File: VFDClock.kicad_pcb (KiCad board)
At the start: 2 copper layers, 68.6 x 53.3 mm, 8 parts, among them P1 Power, P2 Analog, P3 Digital, P4 Digital, P5 CONN_01X01, P6 CONN_01X01, P7 CONN_01X01, P8 CONN_01X01

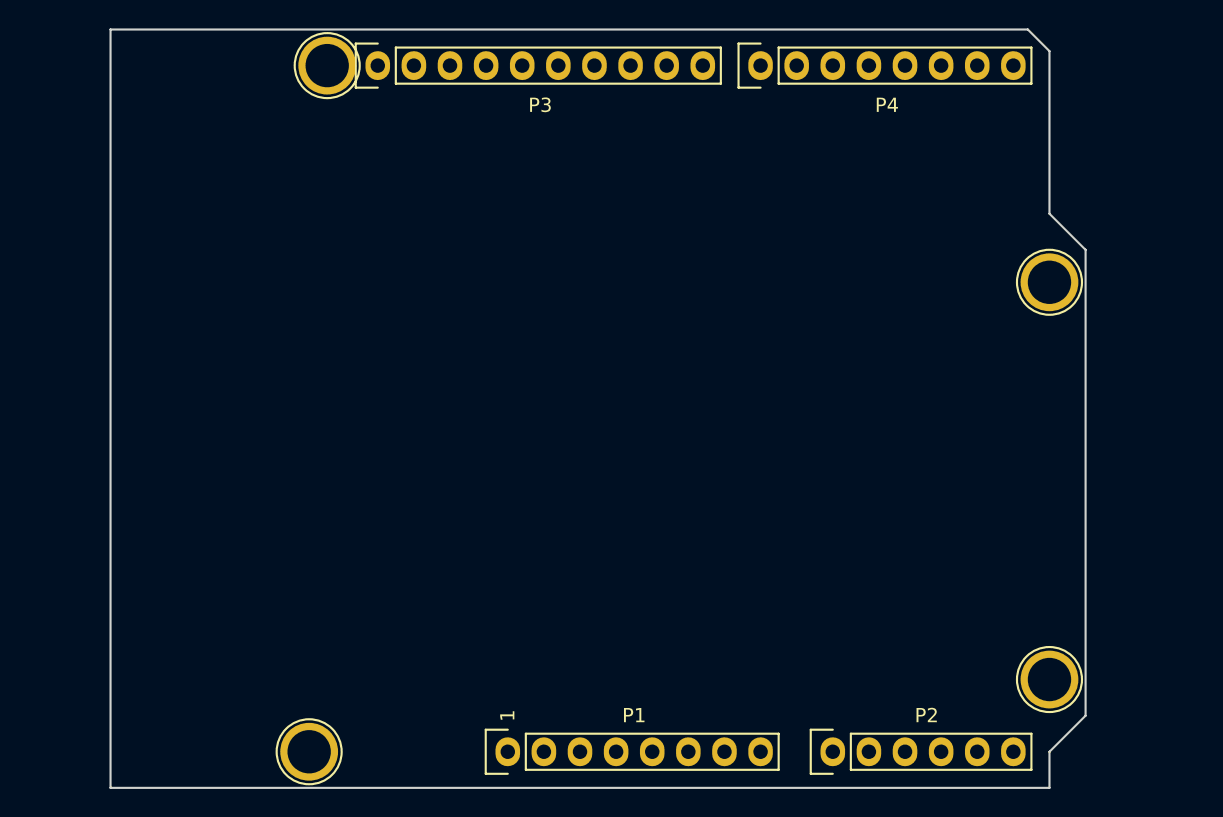
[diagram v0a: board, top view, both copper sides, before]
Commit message: VFDとICをつないだ回路を作成
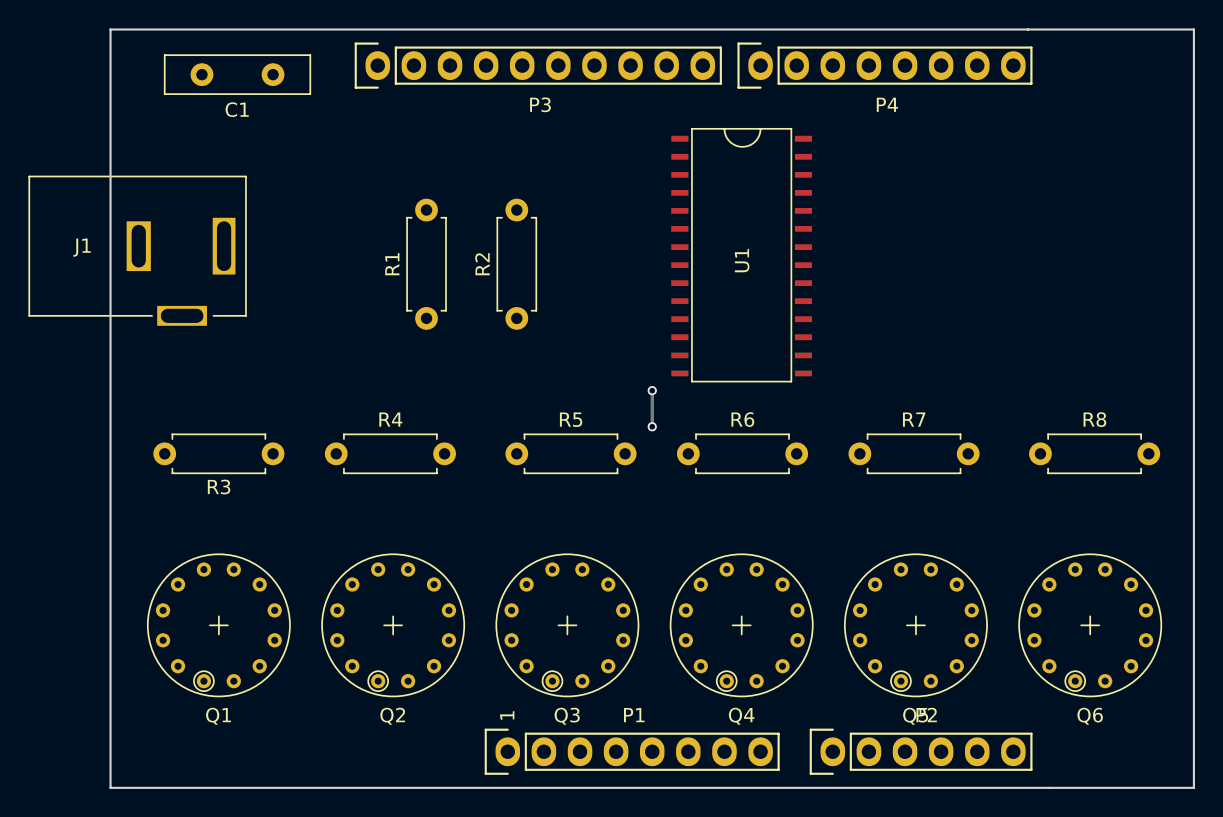
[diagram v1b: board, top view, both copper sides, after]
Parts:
- removed P5, P6, P7, P8: CONN_01X01, Socket_Arduino_Uno:Arduino_1pin
- added C1: 0.1u, Capacitor_THT:C_Disc_D10.0mm_W2.5mm_P5.00mm, F.Cu at (122.4, 76.2)
- added J1: Barrel_Jack_MountingPin, #MyFootPrints:DCJack_MJ-179PH, F.Cu at (105.3, 88.3)
- added Q1: VFD_LD8035E, #MyFootPrints:VFD_LD8035E, F.Cu at (118.6, 114.9)
- added Q2: VFD_LD8035E, #MyFootPrints:VFD_LD8035E, F.Cu at (130.9, 114.9)
- added Q3: VFD_LD8035E, #MyFootPrints:VFD_LD8035E, F.Cu at (143.1, 114.9)
- added Q4: VFD_LD8035E, #MyFootPrints:VFD_LD8035E, F.Cu at (155.4, 114.9)
- added Q5: VFD_LD8035E, #MyFootPrints:VFD_LD8035E, F.Cu at (167.6, 114.9)
- added Q6: VFD_LD8035E, #MyFootPrints:VFD_LD8035E, F.Cu at (179.9, 114.9)
- added R1: 4.7k, Resistor_THT:R_Axial_DIN0207_L6.3mm_D2.5mm_P7.62mm_Horizontal, F.Cu at (133.2, 93.3)
- added R2: 4.7k, Resistor_THT:R_Axial_DIN0207_L6.3mm_D2.5mm_P7.62mm_Horizontal, F.Cu at (139.6, 93.3)
- added R3: 560, Resistor_THT:R_Axial_DIN0207_L6.3mm_D2.5mm_P7.62mm_Horizontal, F.Cu at (122.4, 102.9)
- added R4: 560, Resistor_THT:R_Axial_DIN0207_L6.3mm_D2.5mm_P7.62mm_Horizontal, F.Cu at (126.9, 102.9)
- added R5: 560, Resistor_THT:R_Axial_DIN0207_L6.3mm_D2.5mm_P7.62mm_Horizontal, F.Cu at (139.6, 102.9)
- added R6: 560, Resistor_THT:R_Axial_DIN0207_L6.3mm_D2.5mm_P7.62mm_Horizontal, F.Cu at (151.6, 102.9)
- added R7: 560, Resistor_THT:R_Axial_DIN0207_L6.3mm_D2.5mm_P7.62mm_Horizontal, F.Cu at (163.7, 102.9)
- added R8: 560, Resistor_THT:R_Axial_DIN0207_L6.3mm_D2.5mm_P7.62mm_Horizontal, F.Cu at (176.4, 102.9)
- added U1: IC_HT16K33, #MyFootPrints:IC_HT16K33, F.Cu at (151.6, 80.0)
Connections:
- P1 pad 1: Net-(P1-Pad1) -> (no net)
- P1 pad 2: /IOREF -> (no net)
- P1 pad 3: /Reset -> (no net)
- P1 pad 4: +3V3 -> (no net)
- P1 pad 8: /Vin -> +12V
- P2 pad 1: /A0 -> (no net)
- P2 pad 2: /A1 -> (no net)
- P2 pad 3: /A2 -> (no net)
- P2 pad 4: /A3 -> (no net)
- P2 pad 5: /A4(SDA) -> (no net)
- P2 pad 6: /A5(SCL) -> (no net)
- P3 pad 10: /8 -> (no net)
- P3 pad 3: /AREF -> (no net)
- P3 pad 5: /13(SCK) -> (no net)
- P3 pad 6: /12(MISO) -> (no net)
- P3 pad 7: /11(**/MOSI) -> (no net)
- P3 pad 8: /10(**/SS) -> (no net)
- P3 pad 9: /9(**) -> (no net)
- P4 pad 1: /7 -> (no net)
- P4 pad 2: /6(**) -> (no net)
- P4 pad 3: /5(**) -> (no net)
- P4 pad 4: /4 -> (no net)
- P4 pad 5: /3(**) -> (no net)
- P4 pad 6: /2 -> (no net)
- P4 pad 7: /1(Tx) -> (no net)
- P4 pad 8: /0(Rx) -> (no net)
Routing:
- net GND: track 0.00 -> 2.54 mm, vias 0 -> 2
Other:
- board size 68.6 x 53.3 mm -> 76.2 x 53.3 mm
- net class Default: via_dia 0.6 -> 0.65
- net class Power added: clearance 0.2, trace_width 0.6, via_dia 0.65, via_drill 0.4
- rule via_min_size: 0.4 -> 0.65
